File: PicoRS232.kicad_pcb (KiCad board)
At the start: 2 copper layers, 78.7 x 72.9 mm, 34 parts, among them J1 RS232_0, J10 Conn_01x04_Male, J2 RS232_0, J3 RS232_0, J4 RS232_0, J5 RS232_0, J6 RS232_0, J7 Conn_01x06_Male, J8 Conn_01x06_Male, J9 Conn_01x06_Male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

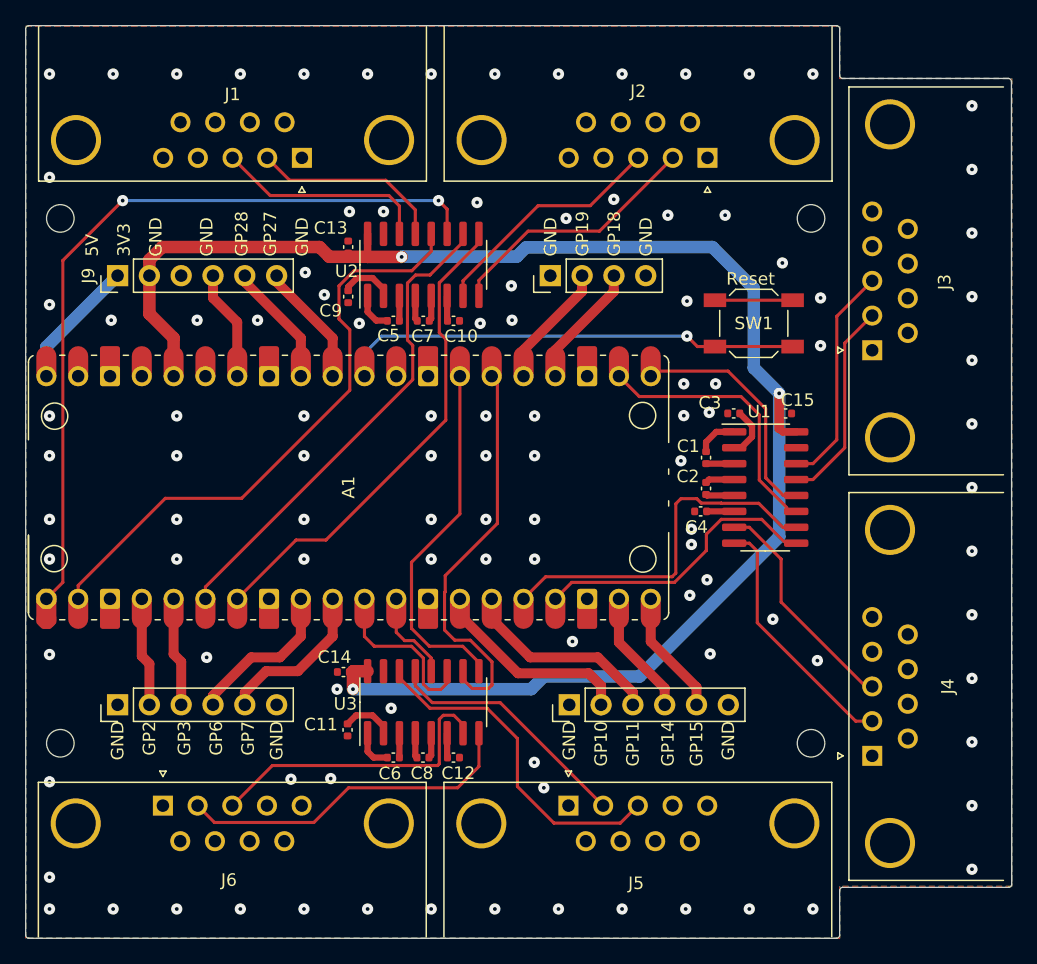
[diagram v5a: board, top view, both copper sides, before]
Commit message: Add silkscreen with name, version, and url.
Also, add pin header part numbers, but leave them out of the BOM.
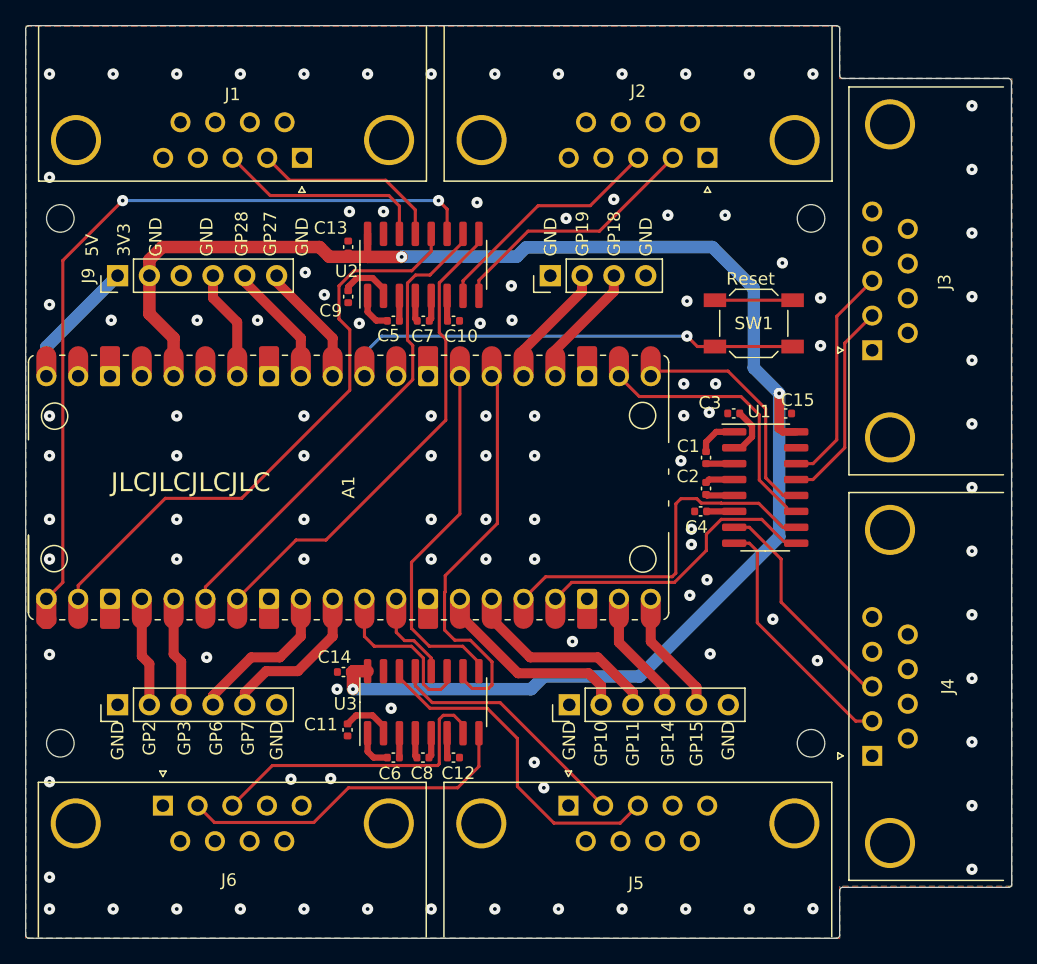
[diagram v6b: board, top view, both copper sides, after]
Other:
- board text added: "${TITLE} ${REVISION} ${COMPANY} ${URL}"
- board text added: "JLCJLCJLCJLC"
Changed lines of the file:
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@@
   )
   (paper "A4")
+  (title_block
+    (title "PicoRS232")
+    (rev "V1.0")
+    (company "Sean D. Cline")
+  )
   (layers
     (0 "F.Cu" signal)
@@
     )
   )
+  (property "COMPANY" "Sean D. Cline")
+  (property "REVISION" "V1.0")
+  (property "TITLE" "PicoRS232")
+  (property "URL" "https://github.com/SeanCline/PicoRS232")
   (net 0 "")
   (net 1 "UART0_TX")
@@
     (descr "Through hole straight pin header, 1x06, 2.54mm pitch, single row")
     (tags "Through hole pin header THT 1x06 2.54mm single row")
+    (property "LCSC" "C225481")
     (property "Sheetfile" "PicoRS232.kicad_sch")
     (property "Sheetname" "")
@@
     (descr "Through hole straight pin header, 1x04, 2.54mm pitch, single row")
     (tags "Through hole pin header THT 1x04 2.54mm single row")
+    (property "LCSC" "C225479")
     (property "Sheetfile" "PicoRS232.kicad_sch")
     (property "Sheetname" "")
@@
     (descr "Through hole straight pin header, 1x06, 2.54mm pitch, single row")
     (tags "Through hole pin header THT 1x06 2.54mm single row")
+    (property "LCSC" "C225481")
     (property "Sheetfile" "PicoRS232.kicad_sch")
     (property "Sheetname" "")
@@
     (descr "Through hole straight pin header, 1x06, 2.54mm pitch, single row")
     (tags "Through hole pin header THT 1x06 2.54mm single row")
+    (property "LCSC" "C225481")
     (property "Sheetfile" "PicoRS232.kicad_sch")
     (property "Sheetname" "")
@@
     (fp_line (start 19.45 41.7) (end 19.45 42.12) (layer "F.SilkS") (width 0.12))
     (fp_line (start -1.67 34.08) (end -1.67 34.5) (layer "F.SilkS") (width 0.12))
-    (fp_arc (start 19.42 49.32) (mid 19.213487 49.588772) (end 18.89 49.69) (layer "F.SilkS") (width 0.12))
+    (fp_arc (start 19.42 49.32) (mid 19.213497 49.588778) (end 18.89 49.69) (layer "F.SilkS") (width 0.12))
     (fp_arc (start -1.64 -1.06) (mid -1.433508 -1.328808) (end -1.11 -1.43) (layer "F.SilkS") (width 0.12))
     (fp_arc (start -1.11 49.69) (mid -1.433508 49.588809) (end -1.64 49.32) (layer "F.SilkS") (width 0.12))
@@
   (gr_arc (start 124.46 38.608) (mid 124.639607 38.682393) (end 124.714 38.862) (layer "Edge.Cuts") (width 0.1))
   (gr_arc (start 46.255205 107.262395) (mid 46.0756 107.188) (end 46.001205 107.008395) (layer "Edge.Cuts") (width 0.1))
+  (gr_text "${TITLE} ${REVISION}\n${COMPANY}\n${URL}" (at 109.728 104.14) (layer "B.SilkS")
+    (effects (font (size 1 1) (thickness 0.2)) (justify left mirror))
+  )
   (gr_text "GP18" (at 92.994 52.832 90) (layer "F.SilkS")
     (effects (font (size 1 1) (thickness 0.15)) (justify left))
@@
   (gr_text "GP11" (at 94.488 89.916 90) (layer "F.SilkS")
     (effects (font (size 1 1) (thickness 0.15)) (justify right))
+  )
+  (gr_text "JLCJLCJLCJLC" (at 59.182 70.866) (layer "F.SilkS")
+    (effects (font (size 1.5 1.5) (thickness 0.3)))
   )
   (gr_text "GND" (at 95.534 52.832 90) (layer "F.SilkS")
@@
   (via (at 108.8644 38.2524) (size 0.9) (drill 0.3) (layers "F.Cu" "B.Cu") (free) (net 3))
   (via (at 52.9844 104.9274) (size 0.9) (drill 0.3) (layers "F.Cu" "B.Cu") (free) (net 3))
-  (via (at 108.8644 104.9274) (size 0.9) (drill 0.3) (layers "F.Cu" "B.Cu") (free) (net 3))
+  (via (at 108.8644 104.902) (size 0.9) (drill 0.3) (layers "F.Cu" "B.Cu") (free) (net 3))
   (via (at 121.5644 45.8724) (size 0.9) (drill 0.3) (layers "F.Cu" "B.Cu") (free) (net 3))
   (via (at 78.3844 73.8124) (size 0.9) (drill 0.3) (layers "F.Cu" "B.Cu") (free) (net 3))
